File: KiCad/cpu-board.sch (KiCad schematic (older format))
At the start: 56 parts, among them CON1 BARREL_JACK, J1 Conn_FT245R, SW1 SW_PUSH_SMALL, SW2 SW_PUSH_SMALL, SW3 SWITCH_INV, U1 29F040B, U10 74LS377, U11 GAL22V10, U2 68008D, U3 74LS00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

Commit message: annotate pull-up resistors
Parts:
- gave numbers to parts that had none: 2
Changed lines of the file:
@@
 	6000 4550 6050 4550
 $Comp
-L cpu-board-rescue:R R?
+L cpu-board-rescue:R R15
 U 1 1 5E78BFBC
 P 5800 4300
-F 0 "R?" V 5880 4300 40  0000 C CNN
+F 0 "R15" V 5880 4300 40  0000 C CNN
 F 1 "10K" V 5800 4300 40  0000 C CNN
 F 2 "Discret:R3-5" V 5730 4300 30  0001 C CNN
@@
 $EndComp
 $Comp
-L cpu-board-rescue:R R?
+L cpu-board-rescue:R R16
 U 1 1 5E7D729D
 P 5800 4500
-F 0 "R?" V 5880 4500 40  0000 C CNN
+F 0 "R16" V 5880 4500 40  0000 C CNN
 F 1 "10K" V 5800 4500 40  0000 C CNN
 F 2 "Discret:R3-5" V 5730 4500 30  0001 C CNN

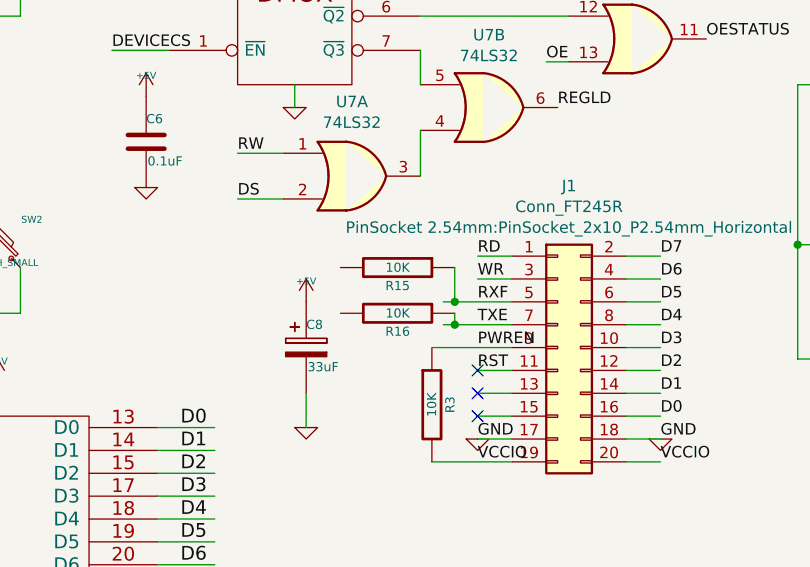
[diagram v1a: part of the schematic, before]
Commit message: connect pull-ups to +5V
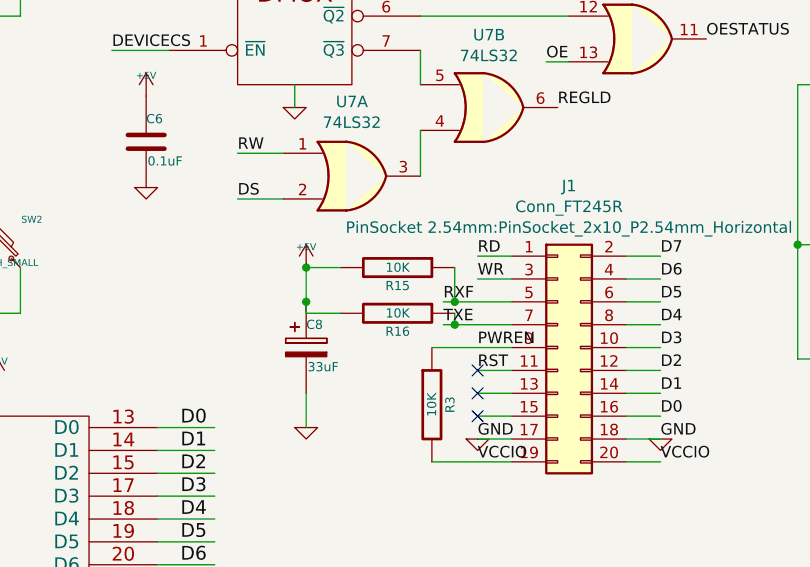
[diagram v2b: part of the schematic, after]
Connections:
- wire segments 278 -> 282
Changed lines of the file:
@@
 L power:+5V #PWR021
 U 1 1 548819AF
-P 5400 4450
-F 0 "#PWR021" H 5400 4540 20  0001 C CNN
-F 1 "+5V" H 5400 4540 30  0000 C CNN
-F 2 "" H 5400 4450 60  0000 C CNN
-F 3 "" H 5400 4450 60  0000 C CNN
-	1    5400 4450
+P 5400 4300
+F 0 "#PWR021" H 5400 4390 20  0001 C CNN
+F 1 "+5V" H 5400 4390 30  0000 C CNN
+F 2 "" H 5400 4300 60  0000 C CNN
+F 3 "" H 5400 4300 60  0000 C CNN
+	1    5400 4300
 	1    0    0    -1
 $EndComp
@@
 Text Label 6150 4350 0    50   ~ 0
 WR
-Text Label 6150 4450 0    50   ~ 0
+Text Label 6000 4450 0    50   ~ 0
 RXF
-Text Label 6150 4550 0    50   ~ 0
+Text Label 6000 4550 0    50   ~ 0
 TXE
 Text Label 6150 4650 0    50   ~ 0
@@
 Wire Wire Line
 	6050 4550 6300 4550
+Wire Wire Line
+	5400 4450 5400 4300
+Wire Wire Line
+	5400 4300 5550 4300
+Connection ~ 5400 4300
+Wire Wire Line
+	5550 4500 5400 4500
+Wire Wire Line
+	5400 4500 5400 4450
+Connection ~ 5400 4450
 $EndSCHEMATC

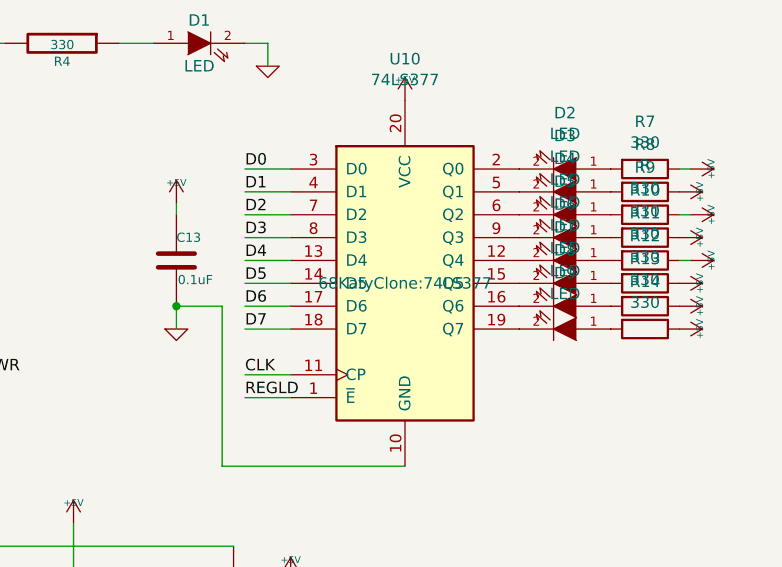
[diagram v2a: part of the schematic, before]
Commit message: associate 20-pin TTL 377 and 244 with long-pad socket footprints
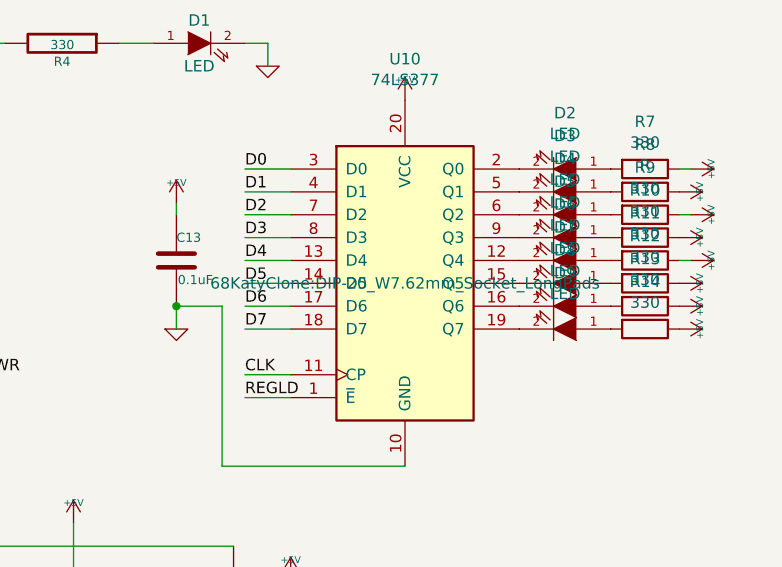
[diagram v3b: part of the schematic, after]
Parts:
- U10: footprint 68KatyClone:74LS377 -> 68KatyClone:DIP-20_W7.62mm_Socket_LongPads
- U8: footprint (none) -> 68KatyClone:DIP-20_W7.62mm_Socket_LongPads
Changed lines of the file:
@@
 F 0 "U10" H 9750 3031 50  0000 C CNN
 F 1 "74LS377" H 9750 2940 50  0000 C CNN
-F 2 "68KatyClone:74LS377" H 9750 2050 50  0000 C CNN
+F 2 "68KatyClone:DIP-20_W7.62mm_Socket_LongPads" H 9750 2050 50  0000 C CNN
 F 3 "http://www.ti.com/lit/gpn/sn74LS377" H 9750 2050 50  0001 C CNN
 	1    9750 2050
@@
 F 0 "U8" H 6300 7931 50  0000 C CNN
 F 1 "74LS244" H 6300 7840 50  0000 C CNN
-F 2 "" H 6300 6950 50  0001 C CNN
+F 2 "68KatyClone:DIP-20_W7.62mm_Socket_LongPads" H 6300 6950 50  0001 C CNN
 F 3 "http://www.ti.com/lit/gpn/sn74LS244" H 6300 6950 50  0001 C CNN
 	1    6300 6950
